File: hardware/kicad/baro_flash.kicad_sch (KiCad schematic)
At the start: 10 parts, among them U401 DPS368XTSA1, U402 W25Q128JVSIQ

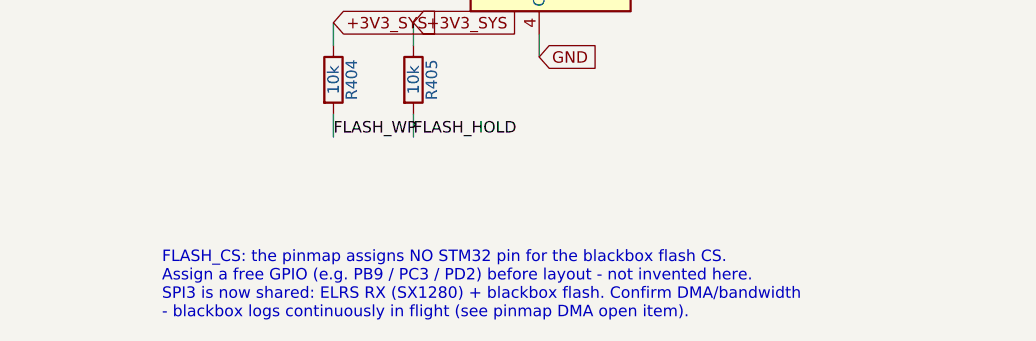
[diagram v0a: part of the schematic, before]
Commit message: Apply SPI-ELRS removal: FLASH_CS=PA15, RX_UART on PB10/PB11, PB13-15 spare
Co-Authored-By: Claude Sonnet 5 <noreply@anthropic.com>
Claude-Session: https://claude.ai/code/session_01JDQYoFvbjRHNSgGtfc2pWo
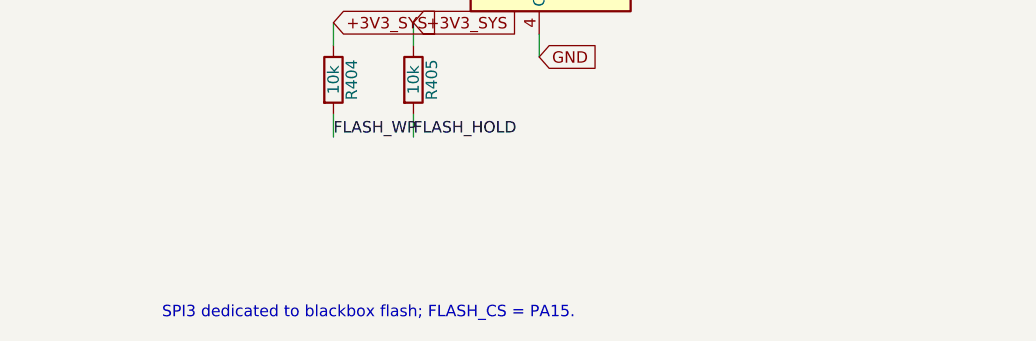
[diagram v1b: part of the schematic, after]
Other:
- note added: "SPI3 dedicated to blackbox flash; FLASH_CS = PA15."
- note removed: "FLASH_CS: the pinmap assigns NO STM32 pin for the blackbox flash CS. Assign a free GPIO (e.g. PB9 / PC3 / PD2) before layout - not invented here. SPI3 is now shared: ELRS RX (SX1280) + blackbox flash. Confirm DMA/bandwidth - blackbox logs continuously in flight (see pinmap DMA open item)."
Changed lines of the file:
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@@
     (effects (font (size 1.27 1.27)) (justify left bottom))
   )
-  (text "FLASH_CS: the pinmap assigns NO STM32 pin for the blackbox flash CS.\nAssign a free GPIO (e.g. PB9 / PC3 / PD2) before layout - not invented here.\nSPI3 is now shared: ELRS RX (SX1280) + blackbox flash. Confirm DMA/bandwidth\n- blackbox logs continuously in flight (see pinmap DMA open item)."
+  (text "SPI3 dedicated to blackbox flash; FLASH_CS = PA15."
     (at 168.91 185.42 0)
     (effects (font (size 1.27 1.27)) (justify left bottom))
